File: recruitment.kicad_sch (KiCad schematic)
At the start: 1 part

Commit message: remove template placeholder
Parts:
- removed C1: 1F, Capacitor_SMD:C_0805_2012Metric, symbol Device:C
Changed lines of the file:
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@@
-(kicad_sch (version 20211123) (generator eeschema)
-  (paper "A4")
-  (title_block
-    (title "Template")
-    (date "2022-04-19")
-    (rev "V0")
-    (company "E-Agle TRT")
-  )
-  (wire (pts (xy 199.39 121.92) (xy 193.04 121.92))
-    (stroke (width 0) (type default) (color 0 0 0 0))
-  )
-  (wire (pts (xy 193.04 121.92) (xy 193.04 130.81))
-    (stroke (width 0) (type default) (color 0 0 0 0))
-  )
-  (wire (pts (xy 199.39 130.81) (xy 199.39 129.54))
-    (stroke (width 0) (type default) (color 0 0 0 0))
-  )
-  (wire (pts (xy 193.04 130.81) (xy 199.39 130.81))
-    (stroke (width 0) (type default) (color 0 0 0 0))
-  )
-  (symbol (lib_id "Device:C") (at 199.39 125.73 0) (unit 1)
-    (in_bom yes) (on_board yes) (fields_autoplaced)
-    (property "Reference" "C1" (id 0) (at 203.2 124.4599 0)
-      (effects (font (size 1.27 1.27)) (justify left))
-    )
-    (property "Value" "1F" (id 1) (at 203.2 126.9999 0)
-      (effects (font (size 1.27 1.27)) (justify left))
-    )
-    (property "Footprint" "Capacitor_SMD:C_0805_2012Metric" (id 2) (at 200.3552 129.54 0)
-      (effects (font (size 1.27 1.27)) hide)
-    )
-    (property "Datasheet" "~" (id 3) (at 199.39 125.73 0)
-      (effects (font (size 1.27 1.27)) hide)
-    )
-    (pin "1")
-    (pin "2")
-  )
-  (sheet_instances
-    (path "/" (page "1"))
-  )
-  (symbol_instances
-    (path "/34d03349-6d78-4165-a683-2d8b76f2bae8"
-      (reference "C1") (unit 1) (value "1F") (footprint "Capacitor_SMD:C_0805_2012Metric")
-    )
-  )
+(kicad_sch
+	(version 20260306)
+	(generator "eeschema")
+	(generator_version "10.0")
+	(paper "A4")
+	(title_block
+		(title "Template")
+		(date "2022-04-19")
+		(rev "V0")
+		(company "E-Agle TRT")
+	)
+	(sheet_instances
+		(path "/"
+			(page "1")
+		)
+	)
+	(embedded_fonts no)
 )

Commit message: Set schematic title block
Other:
- title: Template -> 500 W Overcurrent Monitor
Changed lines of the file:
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@@
 	(paper "A4")
 	(title_block
-		(title "Template")
-		(date "2022-04-19")
-		(rev "V0")
+		(title "500 W Overcurrent Monitor")
+		(date "2026-10-01")
+		(rev "A")
 		(company "E-Agle TRT")
+		(comment 1 "Author: Gabriel Chuffart")
+		(comment 2 "Electronics recruitment test")
 	)
 	(sheet_instances

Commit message: Add hierarchical sheet structure
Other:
- added sheet Power (power.kicad_sch)
- added sheet Relay (relay.kicad_sch)
- added sheet Sensing (sensing.kicad_sch)
- added sheet Trip Logic (trip_logic.kicad_sch)

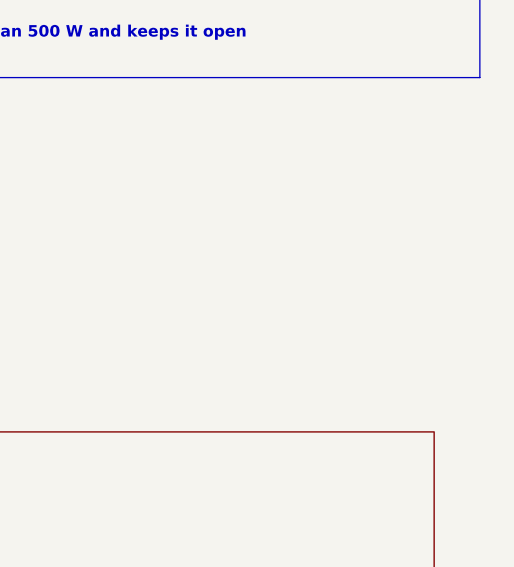
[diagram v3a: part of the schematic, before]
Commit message: Fix relay symbol link, add load terminals and mounting holes
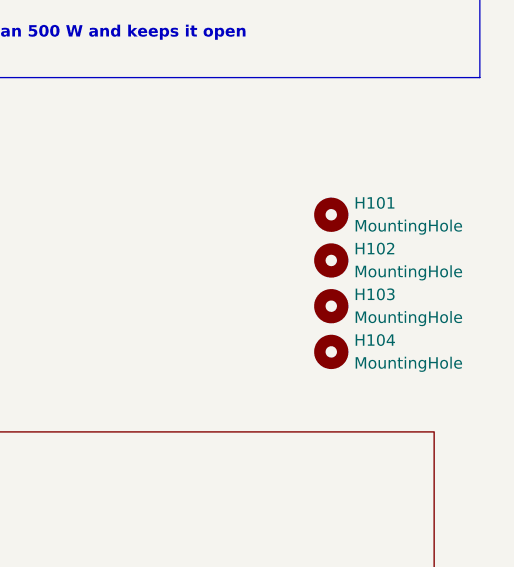
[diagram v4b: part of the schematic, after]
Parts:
- added H101, H102, H103, H104: MountingHole, MountingHole:MountingHole_3.2mm_M3, symbol Mechanical:MountingHole
